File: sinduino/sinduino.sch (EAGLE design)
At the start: 33 parts, among them IC1 IC_UC_ATMEGA32U4-TQFP44, IC2 TS2940CT5TV, Q1 16000, X1 MINI-USB-32005-301

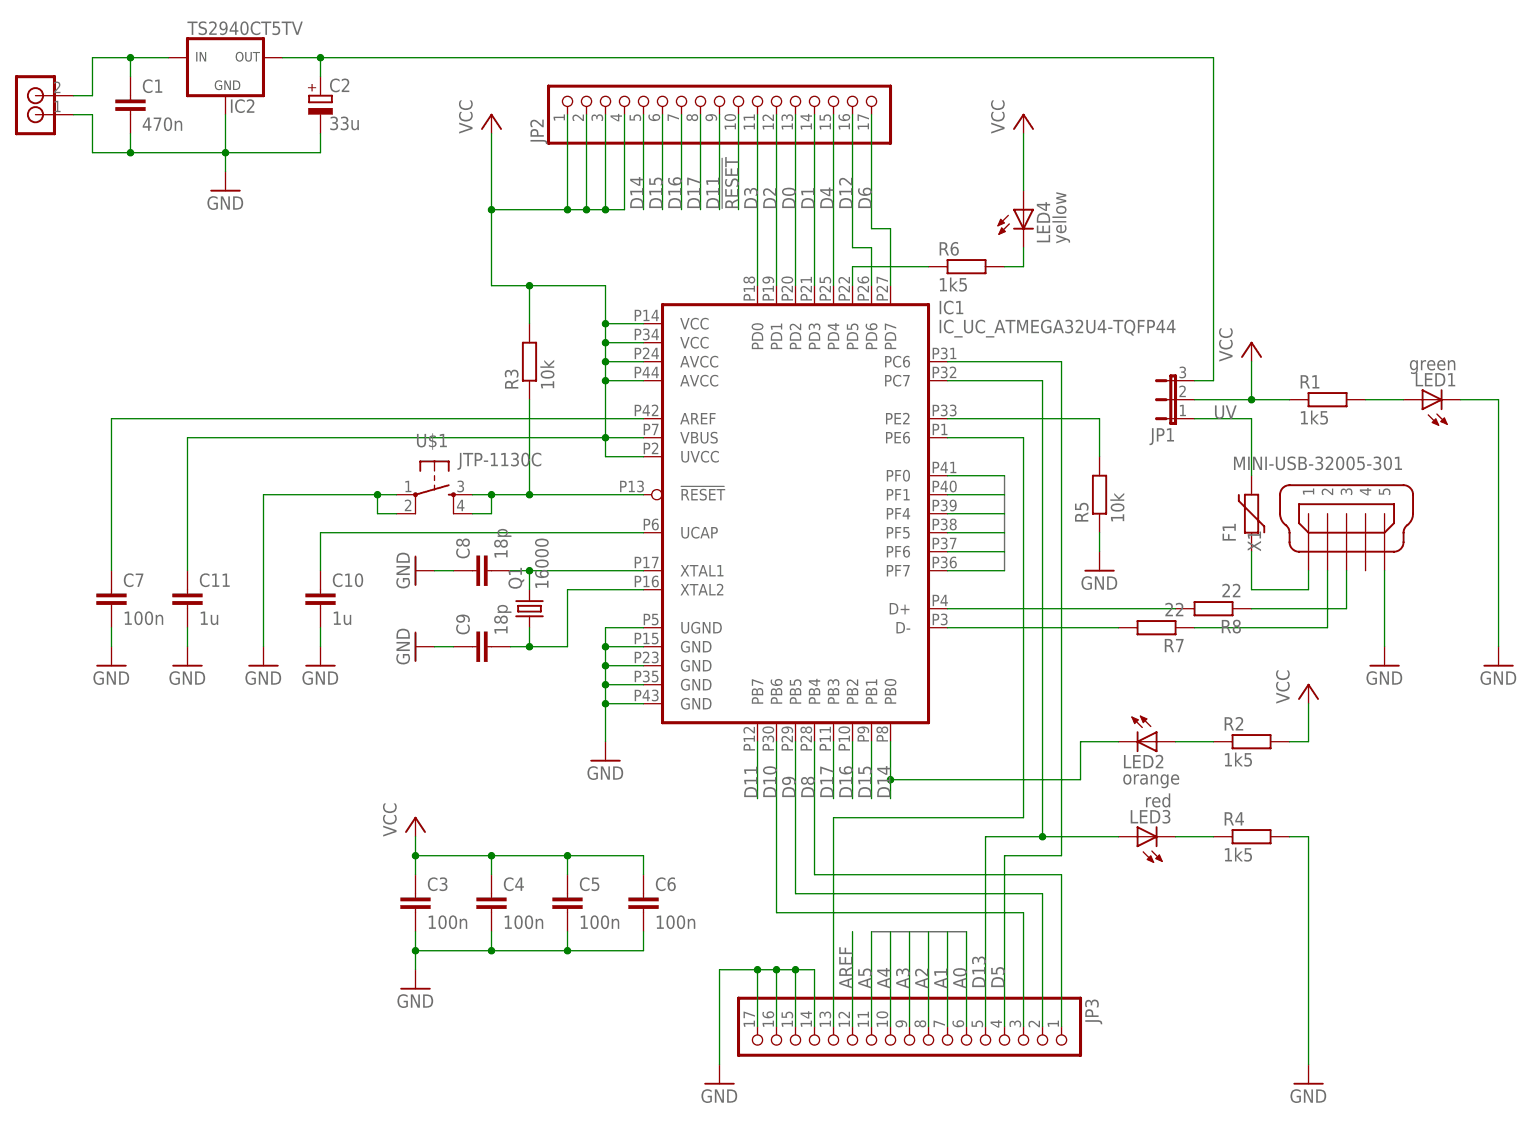
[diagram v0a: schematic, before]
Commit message: replace mini usb connector and fix #3
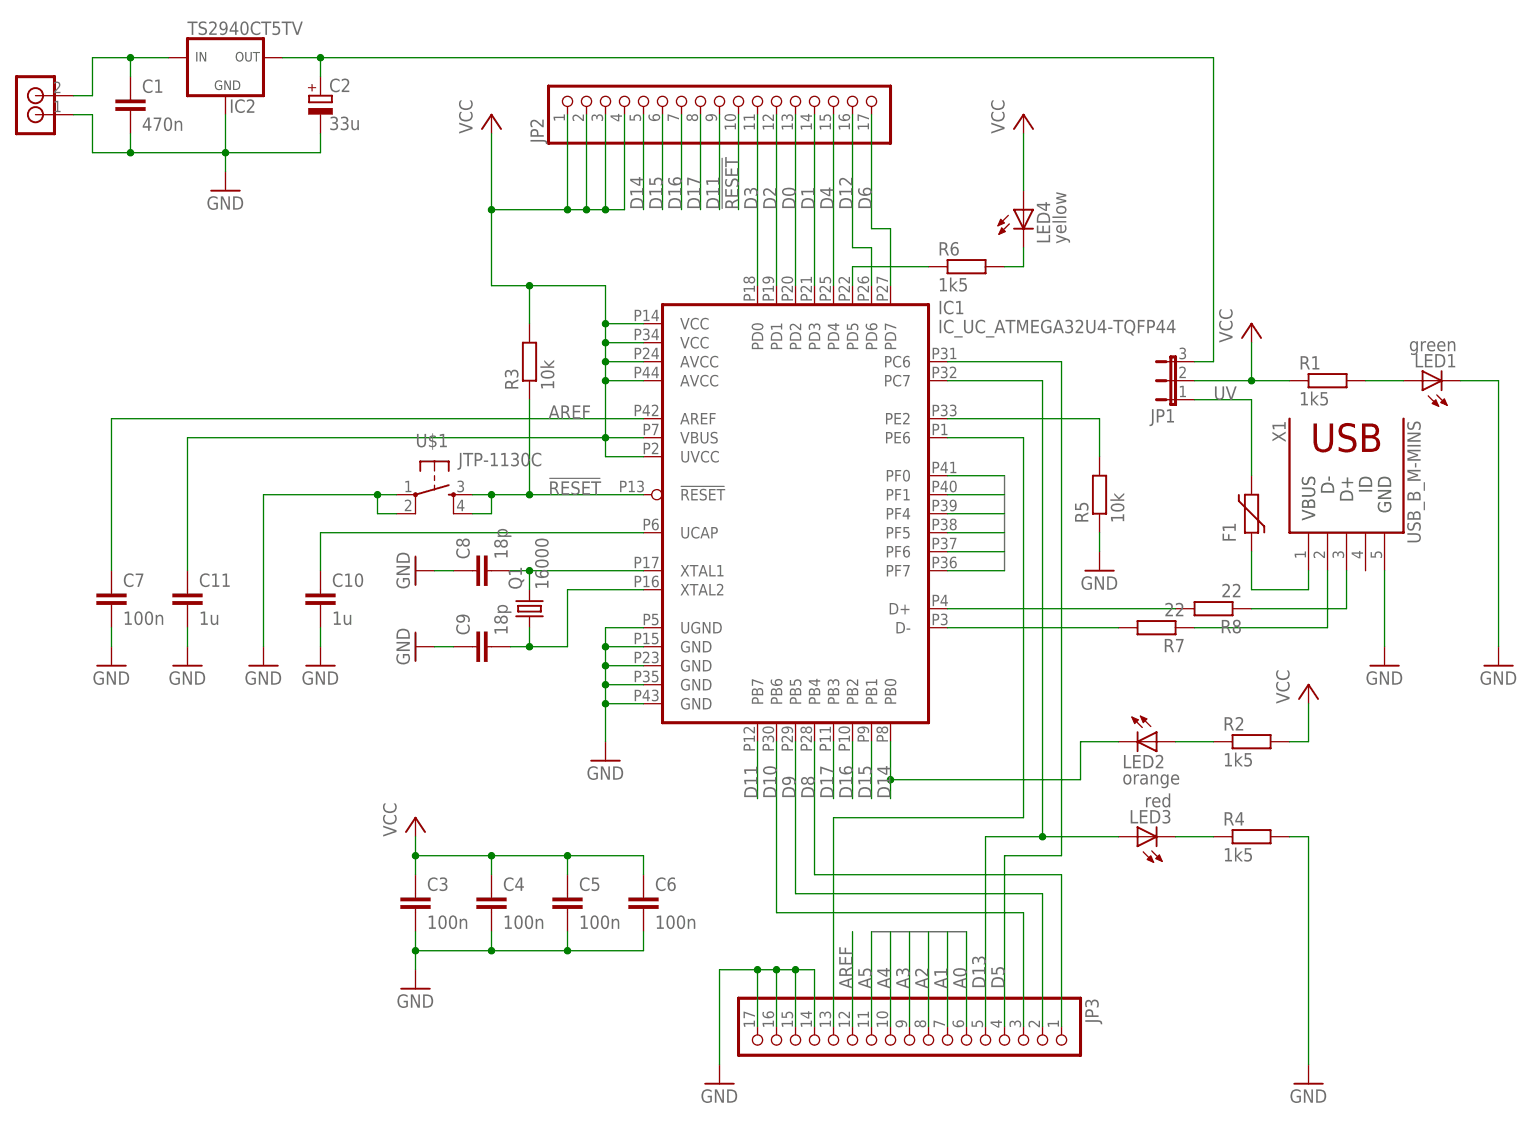
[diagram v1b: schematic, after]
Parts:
- X1: value MINI-USB-32005-301 -> USB_B_M-MINS; device con-cypressindustries:MINI-USB-32005-301 -> n39:USB_B_M-MINS
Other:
- moved on the sheet: JP1, LED1, R1
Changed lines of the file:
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@@
 <layer number="97" name="Info" color="7" fill="1" visible="yes" active="yes"/>
 <layer number="98" name="Guide" color="6" fill="1" visible="yes" active="yes"/>
-<layer number="100" name="Muster" color="7" fill="1" visible="yes" active="yes"/>
-<layer number="101" name="Patch_Top" color="7" fill="1" visible="yes" active="yes"/>
-<layer number="102" name="Vscore" color="7" fill="1" visible="yes" active="yes"/>
-<layer number="103" name="ATT_MISO" color="7" fill="1" visible="yes" active="yes"/>
-<layer number="104" name="Name" color="7" fill="1" visible="yes" active="yes"/>
-<layer number="105" name="Beschreib" color="7" fill="1" visible="yes" active="yes"/>
-<layer number="106" name="BGA-Top" color="7" fill="1" visible="yes" active="yes"/>
-<layer number="107" name="BD-Top" color="7" fill="1" visible="yes" active="yes"/>
-<layer number="108" name="centerline" color="7" fill="1" visible="yes" active="yes"/>
-<layer number="116" name="Patch_BOT" color="7" fill="1" visible="yes" active="yes"/>
-<layer number="121" name="_tsilk" color="7" fill="1" visible="yes" active="yes"/>
-<layer number="122" name="_bsilk" color="7" fill="1" visible="yes" active="yes"/>
-<layer number="131" name="prix" color="7" fill="1" visible="yes" active="yes"/>
-<layer number="132" name="test" color="7" fill="1" visible="yes" active="yes"/>
-<layer number="151" name="HeatSink" color="7" fill="1" visible="yes" active="yes"/>
-<layer number="200" name="200bmp" color="7" fill="1" visible="yes" active="yes"/>
-<layer number="201" name="201bmp" color="7" fill="1" visible="yes" active="yes"/>
-<layer number="202" name="202bmp" color="7" fill="1" visible="yes" active="yes"/>
-<layer number="203" name="203bmp" color="7" fill="1" visible="yes" active="yes"/>
-<layer number="204" name="204bmp" color="7" fill="1" visible="yes" active="yes"/>
-<layer number="205" name="205bmp" color="7" fill="1" visible="yes" active="yes"/>
-<layer number="206" name="206bmp" color="7" fill="1" visible="yes" active="yes"/>
-<layer number="207" name="207bmp" color="7" fill="1" visible="yes" active="yes"/>
-<layer number="208" name="208bmp" color="7" fill="1" visible="yes" active="yes"/>
-<layer number="250" name="Descript" color="7" fill="1" visible="yes" active="yes"/>
-<layer number="251" name="SMDround" color="7" fill="1" visible="yes" active="yes"/>
-<layer number="254" name="cooling" color="7" fill="1" visible="yes" active="yes"/>
 </layers>
 <schematic xreflabel="%F%N/%S.%C%R" xrefpart="/%S.%C%R">
@@
 <part name="GND8" library="supply1" deviceset="GND" device=""/>
 <part name="R3" library="rcl" deviceset="R-EU_" device="R1206" value="10k"/>
-<part name="X1" library="con-cypressindustries" deviceset="MINI-USB-" device="32005-301"/>
+<part name="X1" library="n39" deviceset="USB_B_M" device="-MINS"/>
 <part name="GND9" library="supply1" deviceset="GND" device=""/>
 <part name="R7" library="rcl" deviceset="R-EU_" device="R1206" value="22"/>
@@
 <instance part="GND8" gate="1" x="-5.08" y="38.1"/>
 <instance part="R3" gate="G$1" x="30.48" y="78.74" rot="R90"/>
-<instance part="X1" gate="G$1" x="139.7" y="55.88" rot="R90"/>
+<instance part="X1" gate="G$1" x="139.7" y="63.5" rot="MR270"/>
 <instance part="GND9" gate="1" x="144.78" y="38.1"/>
 <instance part="R7" gate="G$1" x="114.3" y="43.18" rot="R180"/>
 <instance part="R8" gate="G$1" x="121.92" y="45.72" rot="R180"/>
 <instance part="F1" gate="G$1" x="127" y="58.42" rot="R90"/>
-<instance part="JP1" gate="1" x="116.84" y="73.66" rot="R90"/>
-<instance part="P+4" gate="VCC" x="127" y="81.28"/>
+<instance part="JP1" gate="1" x="116.84" y="76.2" rot="R90"/>
+<instance part="P+4" gate="VCC" x="127" y="83.82"/>
 <instance part="JP2" gate="G$1" x="53.34" y="114.3" rot="R90"/>
 <instance part="JP3" gate="G$1" x="83.82" y="-12.7" rot="R270"/>
@@
 <instance part="GND12" gate="1" x="-10.16" y="101.6"/>
 <instance part="U$3" gate="G$1" x="-35.56" y="111.76" rot="R180"/>
-<instance part="LED1" gate="G$1" x="149.86" y="73.66" rot="R90"/>
-<instance part="R1" gate="G$1" x="137.16" y="73.66"/>
+<instance part="LED1" gate="G$1" x="149.86" y="76.2" rot="R90"/>
+<instance part="R1" gate="G$1" x="137.16" y="76.2"/>
 <instance part="GND13" gate="1" x="160.02" y="38.1"/>
 <instance part="R2" gate="G$1" x="127" y="27.94"/>
@@
 <pinref part="LED1" gate="G$1" pin="C"/>
 <pinref part="GND13" gate="1" pin="GND"/>
-<wire x1="154.94" y1="73.66" x2="160.02" y2="73.66" width="0.1524" layer="91"/>
-<wire x1="160.02" y1="73.66" x2="160.02" y2="40.64" width="0.1524" layer="91"/>
+<wire x1="154.94" y1="76.2" x2="160.02" y2="76.2" width="0.1524" layer="91"/>
+<wire x1="160.02" y1="76.2" x2="160.02" y2="40.64" width="0.1524" layer="91"/>
 </segment>
 <segment>
@@
 <segment>
 <pinref part="JP1" gate="1" pin="2"/>
-<wire x1="119.38" y1="73.66" x2="127" y2="73.66" width="0.1524" layer="91"/>
-<wire x1="127" y1="73.66" x2="127" y2="78.74" width="0.1524" layer="91"/>
+<wire x1="119.38" y1="76.2" x2="127" y2="76.2" width="0.1524" layer="91"/>
+<wire x1="127" y1="76.2" x2="127" y2="81.28" width="0.1524" layer="91"/>
 <pinref part="P+4" gate="VCC" pin="VCC"/>
 <pinref part="R1" gate="G$1" pin="1"/>
-<wire x1="127" y1="73.66" x2="132.08" y2="73.66" width="0.1524" layer="91"/>
-<junction x="127" y="73.66"/>
+<wire x1="127" y1="76.2" x2="132.08" y2="76.2" width="0.1524" layer="91"/>
+<junction x="127" y="76.2"/>
 </segment>
 <segment>
@@
 <wire x1="30.48" y1="60.96" x2="30.48" y2="73.66" width="0.1524" layer="91"/>
 <junction x="30.48" y="60.96"/>
+<label x="33.02" y="60.96" size="1.778" layer="95"/>
 </segment>
 <segment>
@@
 <segment>
 <pinref part="F1" gate="G$1" pin="2"/>
-<wire x1="127" y1="63.5" x2="127" y2="71.12" width="0.1524" layer="91"/>
-<label x="121.92" y="71.12" size="1.778" layer="95"/>
+<wire x1="127" y1="63.5" x2="127" y2="73.66" width="0.1524" layer="91"/>
+<label x="121.92" y="73.66" size="1.778" layer="95"/>
 <pinref part="JP1" gate="1" pin="1"/>
-<wire x1="119.38" y1="71.12" x2="127" y2="71.12" width="0.1524" layer="91"/>
+<wire x1="119.38" y1="73.66" x2="127" y2="73.66" width="0.1524" layer="91"/>
 </segment>
 </net>
@@
 <wire x1="45.72" y1="71.12" x2="-25.4" y2="71.12" width="0.1524" layer="91"/>
 <wire x1="-25.4" y1="71.12" x2="-25.4" y2="50.8" width="0.1524" layer="91"/>
+<label x="33.02" y="71.12" size="1.778" layer="95"/>
 </segment>
 </net>
@@
 <wire x1="2.54" y1="119.38" x2="2.54" y2="116.84" width="0.1524" layer="91"/>
 <wire x1="2.54" y1="119.38" x2="121.92" y2="119.38" width="0.1524" layer="91"/>
-<wire x1="121.92" y1="119.38" x2="121.92" y2="76.2" width="0.1524" layer="91"/>
+<wire x1="121.92" y1="119.38" x2="121.92" y2="78.74" width="0.1524" layer="91"/>
 <pinref part="JP1" gate="1" pin="3"/>
-<wire x1="121.92" y1="76.2" x2="119.38" y2="76.2" width="0.1524" layer="91"/>
+<wire x1="121.92" y1="78.74" x2="119.38" y2="78.74" width="0.1524" layer="91"/>
 <junction x="2.54" y="119.38"/>
 </segment>
@@
 <pinref part="R1" gate="G$1" pin="2"/>
 <pinref part="LED1" gate="G$1" pin="A"/>
-<wire x1="142.24" y1="73.66" x2="147.32" y2="73.66" width="0.1524" layer="91"/>
+<wire x1="142.24" y1="76.2" x2="147.32" y2="76.2" width="0.1524" layer="91"/>
 </segment>
 </net>
@@
 </sheet>
 </sheets>
+<errors>
+</errors>
 </schematic>
 </drawing>

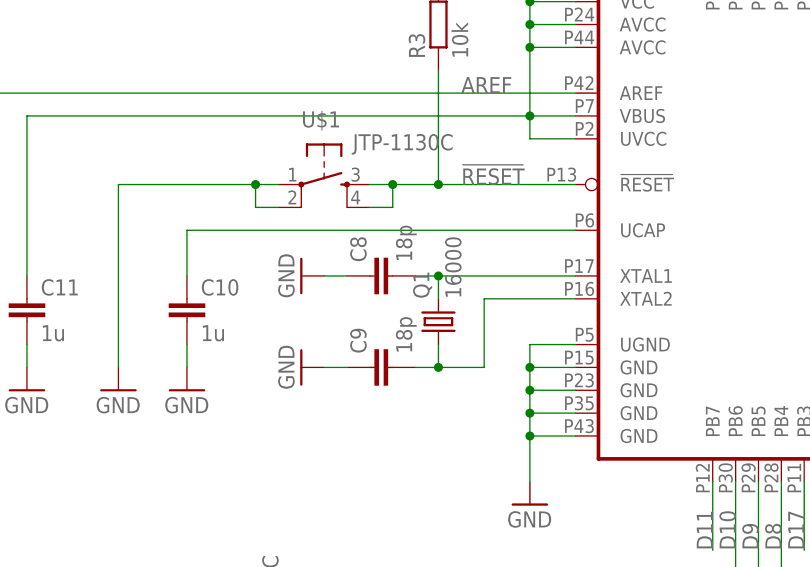
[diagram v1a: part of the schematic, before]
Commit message: change XTAL capicator values to 22p (you can not buy 18p)
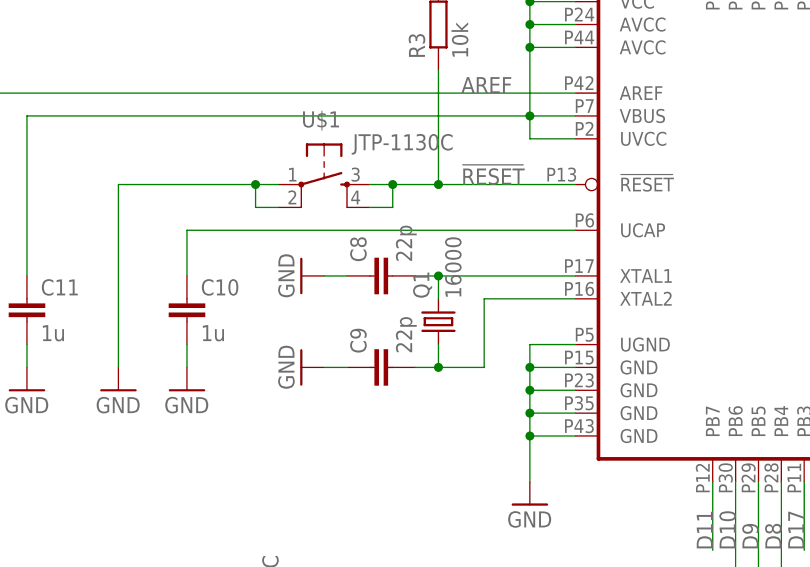
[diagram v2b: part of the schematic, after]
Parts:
- C8, C9: value 18p -> 22p
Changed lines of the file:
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@@
 <part name="C6" library="rcl" deviceset="C-EU" device="C1206" value="100n"/>
 <part name="C7" library="rcl" deviceset="C-EU" device="C1206" value="100n"/>
-<part name="C8" library="rcl" deviceset="C-EU" device="C1206" value="18p"/>
-<part name="C9" library="rcl" deviceset="C-EU" device="C1206" value="18p"/>
+<part name="C8" library="rcl" deviceset="C-EU" device="C1206" value="22p"/>
+<part name="C9" library="rcl" deviceset="C-EU" device="C1206" value="22p"/>
 <part name="C10" library="rcl" deviceset="C-EU" device="C1206" value="1u"/>
 <part name="C11" library="rcl" deviceset="C-EU" device="C1206" value="1u"/>
